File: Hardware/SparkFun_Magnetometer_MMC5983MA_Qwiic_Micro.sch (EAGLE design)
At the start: 26 parts, among them J1 QWIIC_RIGHT_ANGLE, U2 MMC5983MA_QFN16

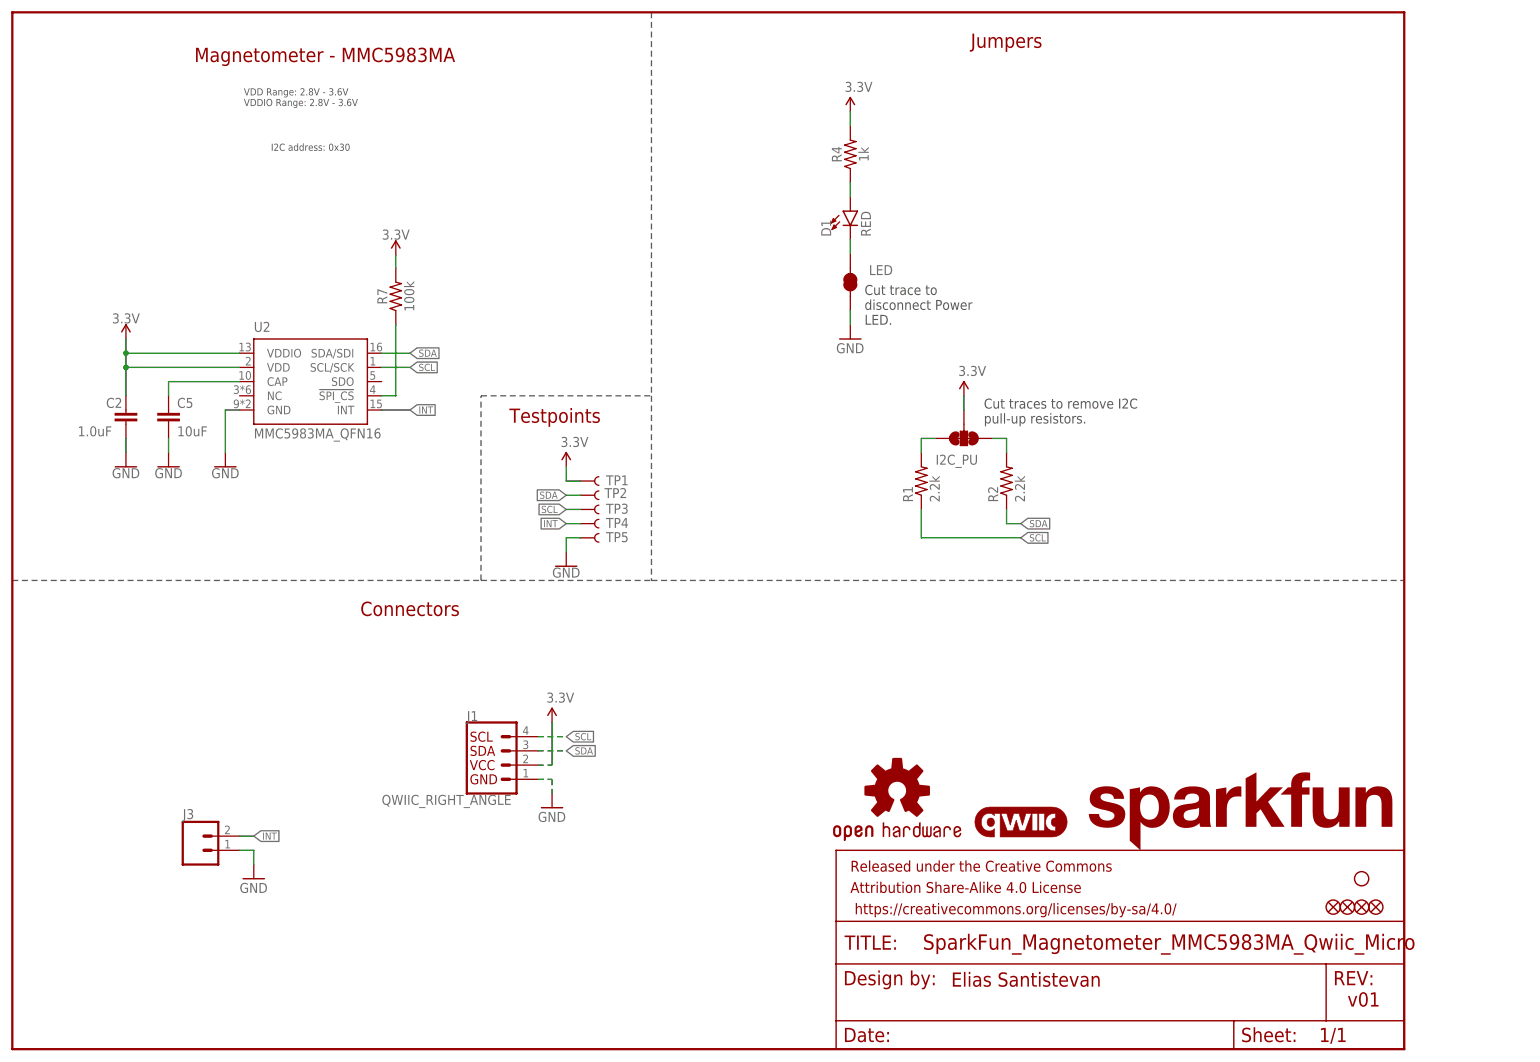
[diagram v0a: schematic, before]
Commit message: Places parts, fixes some schematic alignment issues
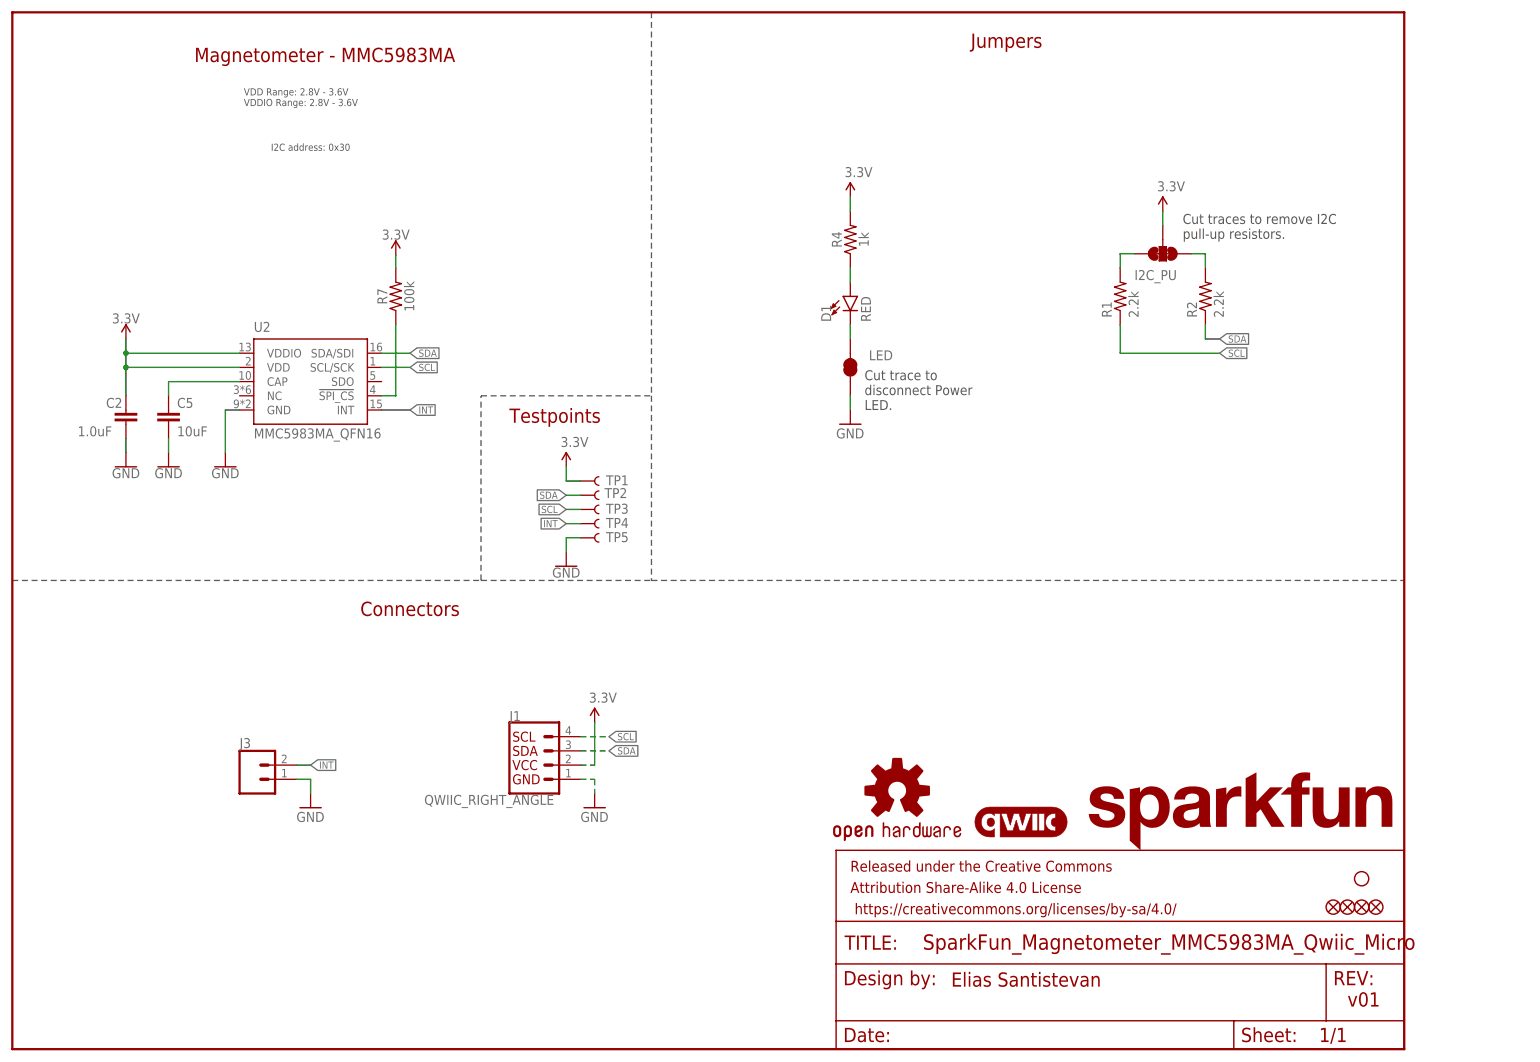
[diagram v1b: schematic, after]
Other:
- moved on the sheet: D1, I2C_PU, J1, J3, LED, R1, R2, R4

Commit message: Routes the board
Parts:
- removed TP4: TEST-POINT3, SparkFun-Connectors:TEST-POINT3
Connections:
- net INT: no longer TP4.1
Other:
- moved on the sheet: TP5
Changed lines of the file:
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@@
 <attribute name="SPICEPREFIX" value="G"/>
 </part>
-<part name="TP4" library="SparkFun-Connectors" deviceset="TEST-POINT" device="3" value="TEST-POINT3"/>
 <part name="TP5" library="SparkFun-Connectors" deviceset="TEST-POINT" device="3" value="TEST-POINT3"/>
 <part name="GND5" library="SparkFun-PowerSymbols" deviceset="GND" device=""/>
@@
 <attribute name="VALUE" x="50.8" y="40.64" size="1.778" layer="96" font="vector"/>
 </instance>
-<instance part="TP4" gate="G$1" x="101.6" y="93.98" smashed="yes">
+<instance part="TP5" gate="G$1" x="101.6" y="93.98" smashed="yes">
 <attribute name="NAME" x="106.172" y="93.218" size="1.778" layer="95" font="vector"/>
 </instance>
-<instance part="TP5" gate="G$1" x="101.6" y="91.44" smashed="yes">
-<attribute name="NAME" x="106.172" y="90.678" size="1.778" layer="95" font="vector"/>
-</instance>
-<instance part="GND5" gate="1" x="99.06" y="86.36" smashed="yes">
-<attribute name="VALUE" x="99.06" y="86.106" size="1.778" layer="96" align="top-center"/>
+<instance part="GND5" gate="1" x="99.06" y="88.9" smashed="yes">
+<attribute name="VALUE" x="99.06" y="88.646" size="1.778" layer="96" align="top-center"/>
 </instance>
 </instances>
@@
 <segment>
 <pinref part="TP5" gate="G$1" pin="1"/>
-<wire x1="99.06" y1="91.44" x2="101.6" y2="91.44" width="0.1524" layer="91"/>
-<wire x1="99.06" y1="91.44" x2="99.06" y2="88.9" width="0.1524" layer="91"/>
+<wire x1="99.06" y1="93.98" x2="101.6" y2="93.98" width="0.1524" layer="91"/>
+<wire x1="99.06" y1="93.98" x2="99.06" y2="91.44" width="0.1524" layer="91"/>
 <pinref part="GND5" gate="1" pin="GND"/>
 </segment>
@@
 <label x="71.12" y="114.3" size="1.27" layer="95" xref="yes"/>
 </segment>
-<segment>
-<pinref part="TP4" gate="G$1" pin="1"/>
-<wire x1="99.06" y1="93.98" x2="101.6" y2="93.98" width="0.1524" layer="91"/>
-<label x="99.06" y="93.98" size="1.27" layer="95" rot="R180" xref="yes"/>
-</segment>
-</net>
+</net>

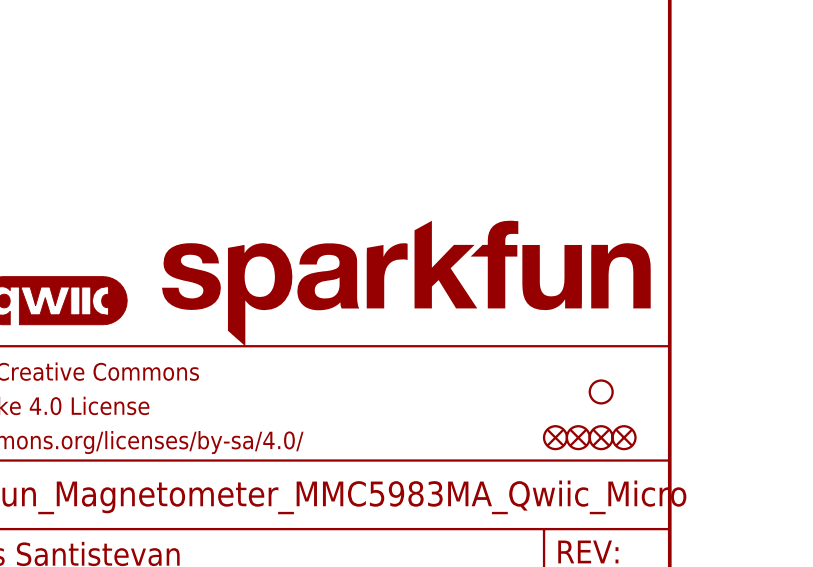
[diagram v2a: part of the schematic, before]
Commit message: Adds Silk, moves testpoints to grid, updates two pin connector
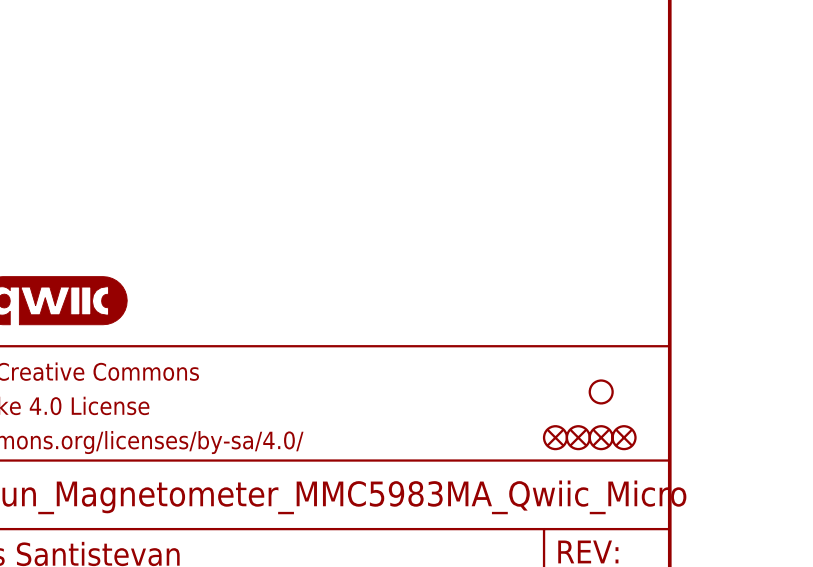
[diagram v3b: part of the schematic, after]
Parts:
- removed LOGO3: SFE_LOGO_NAMEBLANK, SparkFun-Aesthetics:SFE_LOGO_NAMEBLANK
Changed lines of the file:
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@@
 <part name="TP3" library="SparkFun-Connectors" deviceset="TEST-POINT" device="3" value="TEST-POINT3"/>
 <part name="SUPPLY6" library="SparkFun-PowerSymbols" deviceset="3.3V" device=""/>
-<part name="LOGO3" library="SparkFun-Aesthetics" deviceset="SFE_LOGO_NAME" device="BLANK"/>
 <part name="J3" library="SparkFun-Connectors" deviceset="CONN_02" device="_1.5MM"/>
 <part name="U2" library="SparkFun-Sensors" deviceset="MMC5983MA" device="_QFN16"/>
@@
 <attribute name="VALUE" x="98.044" y="107.696" size="1.778" layer="96" font="vector"/>
 </instance>
-<instance part="LOGO3" gate="G$1" x="190.5" y="35.56" smashed="yes"/>
 <instance part="J3" gate="G$1" x="43.18" y="48.26" smashed="yes">
 <attribute name="VALUE" x="40.64" y="43.434" size="1.778" layer="96" font="vector"/>

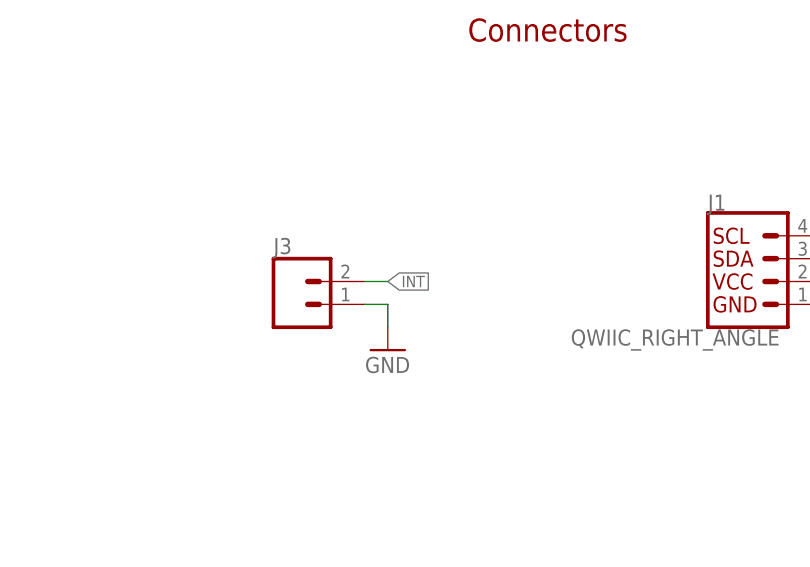
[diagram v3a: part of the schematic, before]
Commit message: Moves interrupt and ground pins, fixes silk, moves testpoints to 0.0375" grid
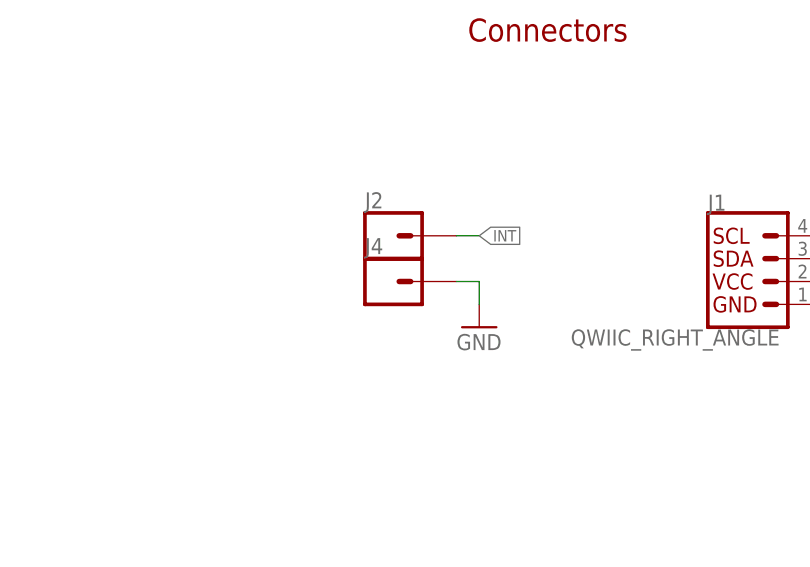
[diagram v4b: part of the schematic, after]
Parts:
- removed J3: (no value), SparkFun-Connectors:CONN_02_1.5MM
- added J2, J4: (no value), SparkFun-Connectors:CONN_01_1MM
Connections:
- net GND: now also J4.1; no longer J3.1
- net INT: now also J2.1; no longer J3.2
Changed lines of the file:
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@@
 <part name="TP3" library="SparkFun-Connectors" deviceset="TEST-POINT" device="3" value="TEST-POINT3"/>
 <part name="SUPPLY6" library="SparkFun-PowerSymbols" deviceset="3.3V" device=""/>
-<part name="J3" library="SparkFun-Connectors" deviceset="CONN_02" device="_1.5MM"/>
 <part name="U2" library="SparkFun-Sensors" deviceset="MMC5983MA" device="_QFN16"/>
 <part name="SUPPLY8" library="SparkFun-PowerSymbols" deviceset="3.3V" device=""/>
@@
 <part name="R7" library="SparkFun-Resistors" deviceset="100KOHM" device="-0402T-1/16W-1%" value="100k"/>
 <part name="SUPPLY9" library="SparkFun-PowerSymbols" deviceset="3.3V" device=""/>
-<part name="GND4" library="SparkFun-PowerSymbols" deviceset="GND" device="">
+<part name="TP5" library="SparkFun-Connectors" deviceset="TEST-POINT" device="3" value="TEST-POINT3"/>
+<part name="GND5" library="SparkFun-PowerSymbols" deviceset="GND" device=""/>
+<part name="J2" library="SparkFun-Connectors" deviceset="CONN_01" device="_1MM"/>
+<part name="J4" library="SparkFun-Connectors" deviceset="CONN_01" device="_1MM"/>
+<part name="GND6" library="SparkFun-PowerSymbols" deviceset="GND" device="">
 <attribute name="SPICEPREFIX" value="G"/>
 </part>
-<part name="TP5" library="SparkFun-Connectors" deviceset="TEST-POINT" device="3" value="TEST-POINT3"/>
-<part name="GND5" library="SparkFun-PowerSymbols" deviceset="GND" device=""/>
 </parts>
 <sheets>
@@
 <attribute name="VALUE" x="98.044" y="107.696" size="1.778" layer="96" font="vector"/>
 </instance>
-<instance part="J3" gate="G$1" x="43.18" y="48.26" smashed="yes">
-<attribute name="VALUE" x="40.64" y="43.434" size="1.778" layer="96" font="vector"/>
-<attribute name="NAME" x="40.64" y="53.848" size="1.778" layer="95" font="vector"/>
-</instance>
 <instance part="U2" gate="G$1" x="43.18" y="111.76" smashed="yes">
 <attribute name="NAME" x="43.18" y="128.27" size="1.778" layer="95"/>
@@
 <attribute name="VALUE" x="68.58" y="144.78" size="1.778" layer="96" align="bottom-center"/>
 </instance>
-<instance part="GND4" gate="1" x="53.34" y="43.18" smashed="yes">
-<attribute name="VALUE" x="50.8" y="40.64" size="1.778" layer="96" font="vector"/>
-</instance>
 <instance part="TP5" gate="G$1" x="101.6" y="93.98" smashed="yes">
 <attribute name="NAME" x="106.172" y="93.218" size="1.778" layer="95" font="vector"/>
@@
 <instance part="GND5" gate="1" x="99.06" y="88.9" smashed="yes">
 <attribute name="VALUE" x="99.06" y="88.646" size="1.778" layer="96" align="top-center"/>
+</instance>
+<instance part="J2" gate="G$1" x="53.34" y="55.88" smashed="yes">
+<attribute name="VALUE" x="50.8" y="51.054" size="1.778" layer="96" font="vector"/>
+<attribute name="NAME" x="50.8" y="58.928" size="1.778" layer="95" font="vector"/>
+</instance>
+<instance part="J4" gate="G$1" x="53.34" y="50.8" smashed="yes">
+<attribute name="VALUE" x="50.8" y="45.974" size="1.778" layer="96" font="vector"/>
+<attribute name="NAME" x="50.8" y="53.848" size="1.778" layer="95" font="vector"/>
+</instance>
+<instance part="GND6" gate="1" x="63.5" y="45.72" smashed="yes">
+<attribute name="VALUE" x="60.96" y="43.18" size="1.778" layer="96" font="vector"/>
 </instance>
 </instances>
@@
 </segment>
 <segment>
-<wire x1="50.8" y1="48.26" x2="53.34" y2="48.26" width="0.1524" layer="91"/>
-<pinref part="GND4" gate="1" pin="GND"/>
-<wire x1="53.34" y1="48.26" x2="53.34" y2="45.72" width="0.1524" layer="91"/>
-<pinref part="J3" gate="G$1" pin="1"/>
-</segment>
-<segment>
 <pinref part="TP5" gate="G$1" pin="1"/>
 <wire x1="99.06" y1="93.98" x2="101.6" y2="93.98" width="0.1524" layer="91"/>
 <wire x1="99.06" y1="93.98" x2="99.06" y2="91.44" width="0.1524" layer="91"/>
 <pinref part="GND5" gate="1" pin="GND"/>
+</segment>
+<segment>
+<wire x1="60.96" y1="50.8" x2="63.5" y2="50.8" width="0.1524" layer="91"/>
+<pinref part="GND6" gate="1" pin="GND"/>
+<wire x1="63.5" y1="50.8" x2="63.5" y2="48.26" width="0.1524" layer="91"/>
+<pinref part="J4" gate="G$1" pin="1"/>
 </segment>
 </net>
@@
 <net name="INT" class="0">
 <segment>
-<wire x1="53.34" y1="50.8" x2="50.8" y2="50.8" width="0.1524" layer="91"/>
-<label x="53.34" y="50.8" size="1.27" layer="95" xref="yes"/>
-<pinref part="J3" gate="G$1" pin="2"/>
-</segment>
-<segment>
 <pinref part="U2" gate="G$1" pin="INT"/>
 <wire x1="66.04" y1="114.3" x2="71.12" y2="114.3" width="0.1524" layer="91"/>
 <label x="71.12" y="114.3" size="1.27" layer="95" xref="yes"/>
 </segment>
-</net>
+<segment>
+<wire x1="63.5" y1="55.88" x2="60.96" y2="55.88" width="0.1524" layer="91"/>
+<label x="63.5" y="55.88" size="1.27" layer="95" xref="yes"/>
+<pinref part="J2" gate="G$1" pin="1"/>
+</segment>
+</net>

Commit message: Adds measures, adds 0402 RED LED from lib
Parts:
- added LOGO3: SFE_LOGO_NAMEBLANK, SparkFun-Aesthetics:SFE_LOGO_NAMEBLANK
- D1: device ISM330DHCX:LED_0402 -> SparkFun-LED:LED-RED_0402
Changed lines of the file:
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@@
 <part name="SUPPLY1" library="SparkFun-PowerSymbols" deviceset="3.3V" device=""/>
 <part name="GND3" library="SparkFun-PowerSymbols" deviceset="GND" device=""/>
-<part name="D1" library="ISM330DHCX" deviceset="LED_0402" device="" value="RED"/>
+<part name="D1" library="SparkFun-LED" deviceset="LED-RED" device="_0402" value="RED"/>
 <part name="R4" library="SparkFun-Resistors" deviceset="1KOHM" device="-0402T-1/16W-1%" value="1k"/>
 <part name="LED" library="SparkFun-Jumpers" deviceset="JUMPER-SMT_2_NC_TRACE" device="_SILK" package3d_urn="urn:adsk.eagle:package:39281/1"/>
@@
 <attribute name="SPICEPREFIX" value="G"/>
 </part>
+<part name="LOGO3" library="SparkFun-Aesthetics" deviceset="SFE_LOGO_NAME" device="BLANK"/>
 </parts>
 <sheets>
@@
 <attribute name="VALUE" x="60.96" y="43.18" size="1.778" layer="96" font="vector"/>
 </instance>
+<instance part="LOGO3" gate="G$1" x="190.5" y="33.02" smashed="yes"/>
 </instances>
 <busses>

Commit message: Increases the size of the silk, fixes measures, rolls to version v10
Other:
- note added: "v10"
- note removed: "v01"
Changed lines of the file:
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@@
 <wire x1="114.3" y1="83.82" x2="248.92" y2="83.82" width="0.2032" layer="97" style="longdash"/>
 <wire x1="114.3" y1="185.42" x2="114.3" y2="116.84" width="0.2032" layer="97" style="longdash"/>
-<text x="238.76" y="7.62" size="2.54" layer="94" font="vector">v01</text>
+<text x="238.76" y="7.62" size="2.54" layer="94" font="vector">v10</text>
 <text x="177.8" y="180.34" size="2.54" layer="94" font="vector" align="center">Jumpers</text>
 <text x="152.4" y="114.3" size="1.778" layer="97" font="vector">Cut trace to
